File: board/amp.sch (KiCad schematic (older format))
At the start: 29 parts, among them J1 GUITAR_IN, J2 POWER, J3 OUT, SW2 SW_DIST, U1 TL071

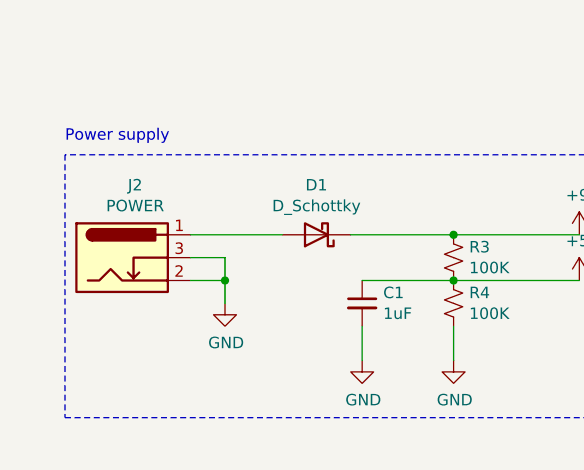
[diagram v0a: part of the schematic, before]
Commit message: Fix board, README corrections
Reverse power jack polarity (make it center-negative), fix typos and
other mistakes in README
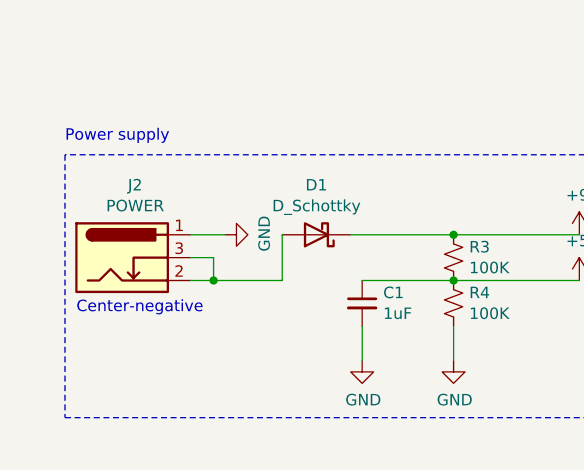
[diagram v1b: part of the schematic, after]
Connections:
- net GND: now also J2.1; no longer J2.2, J2.3
- net at D1.2 (A): now also J2.2, J2.3; no longer J2.1
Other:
- note added: "Center-negative"
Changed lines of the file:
@@
 	1    0    0    -1
 $EndComp
-Wire Wire Line
-	3150 5000 3550 5000
 $Comp
 L power:GND #PWR0101
 U 1 1 5FA73AA2
-P 3300 5300
-F 0 "#PWR0101" H 3300 5050 50  0001 C CNN
-F 1 "GND" H 3305 5127 50  0000 C CNN
-F 2 "" H 3300 5300 50  0001 C CNN
-F 3 "" H 3300 5300 50  0001 C CNN
-	1    3300 5300
-	1    0    0    -1
-$EndComp
-Wire Wire Line
-	3150 5100 3300 5100
-Wire Wire Line
-	3300 5100 3300 5200
-Wire Wire Line
-	3150 5200 3300 5200
-Connection ~ 3300 5200
-Wire Wire Line
-	3300 5200 3300 5300
+P 3300 5000
+F 0 "#PWR0101" H 3300 4750 50  0001 C CNN
+F 1 "GND" H 3305 4827 50  0000 C CNN
+F 2 "" H 3300 5000 50  0001 C CNN
+F 3 "" H 3300 5000 50  0001 C CNN
+	1    3300 5000
+	0    -1   -1   0
+$EndComp
 $Comp
 L power:GND #PWR03
@@
 Text Notes 8050 3000 0    50   ~ 0
 Output jack
+Wire Wire Line
+	3150 5200 3250 5200
+Wire Wire Line
+	3550 5200 3550 5000
+Text Notes 2650 5350 0    50   ~ 0
+Center-negative
+Wire Wire Line
+	3150 5000 3300 5000
+Wire Wire Line
+	3150 5100 3250 5100
+Wire Wire Line
+	3250 5100 3250 5200
+Connection ~ 3250 5200
+Wire Wire Line
+	3250 5200 3550 5200
 $EndSCHEMATC
